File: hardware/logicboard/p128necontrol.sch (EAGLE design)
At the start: 32 parts, among them IC1 74LS595N, IC2 74LS595N, IC3 74LS595N, IC4 74LS595N, IC5 74LS595N, IC6 74LS595N, IC7 74LS595N, IC8 74LS595N

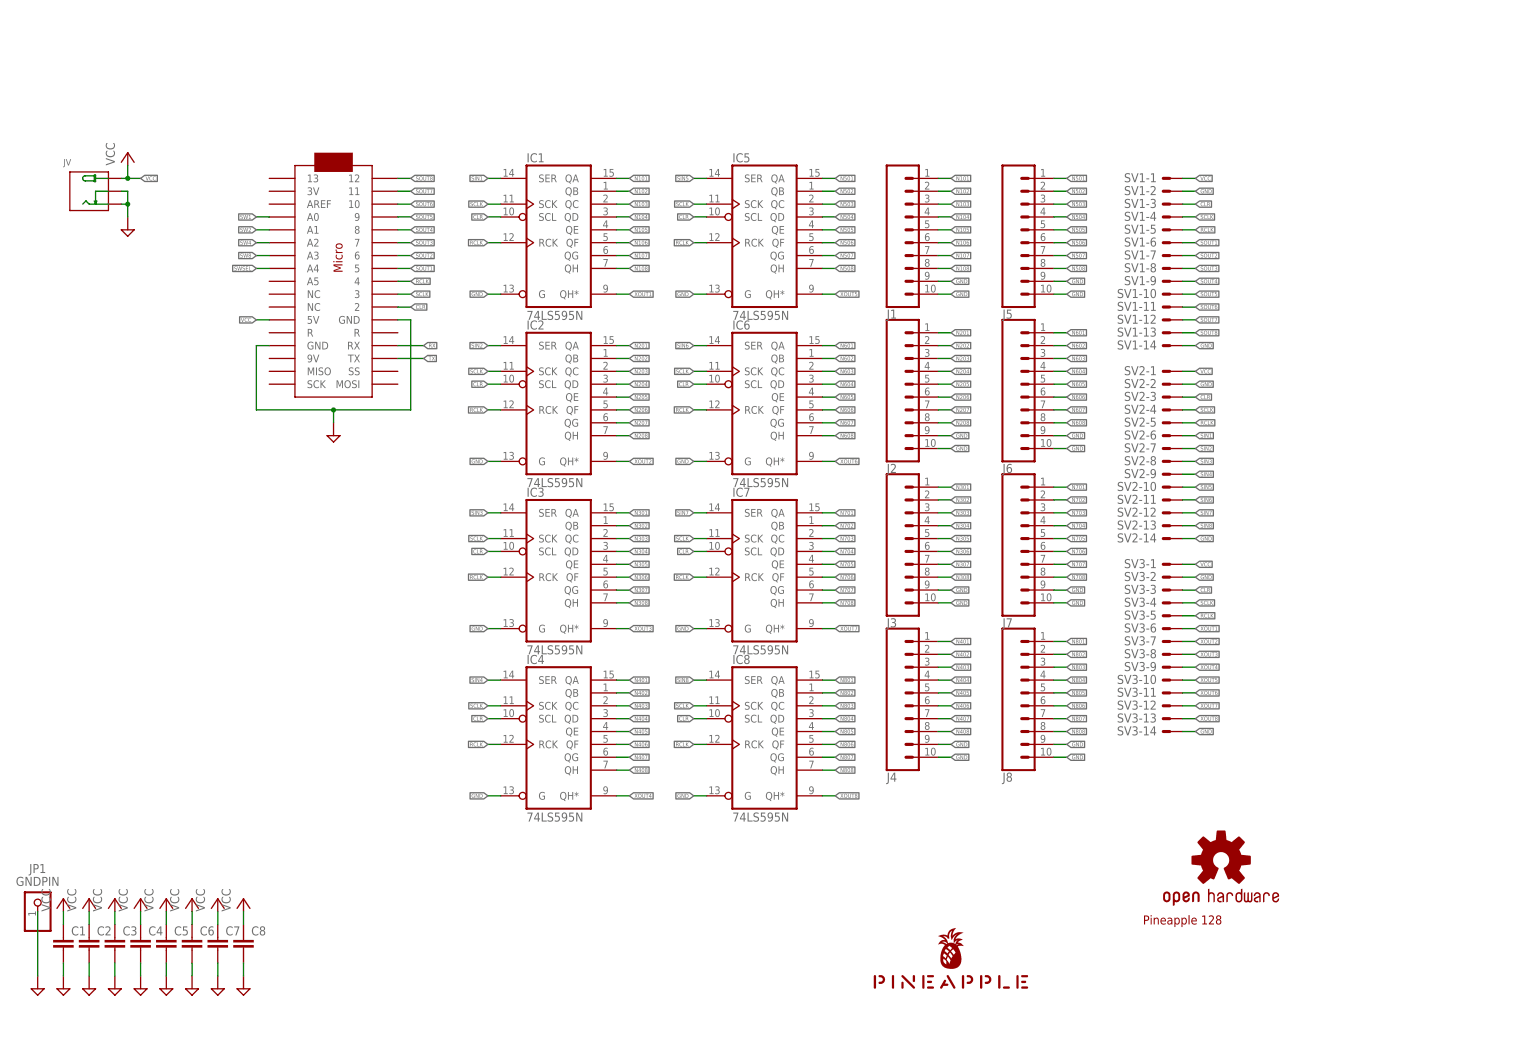
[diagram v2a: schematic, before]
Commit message: Compiled Necontrol.
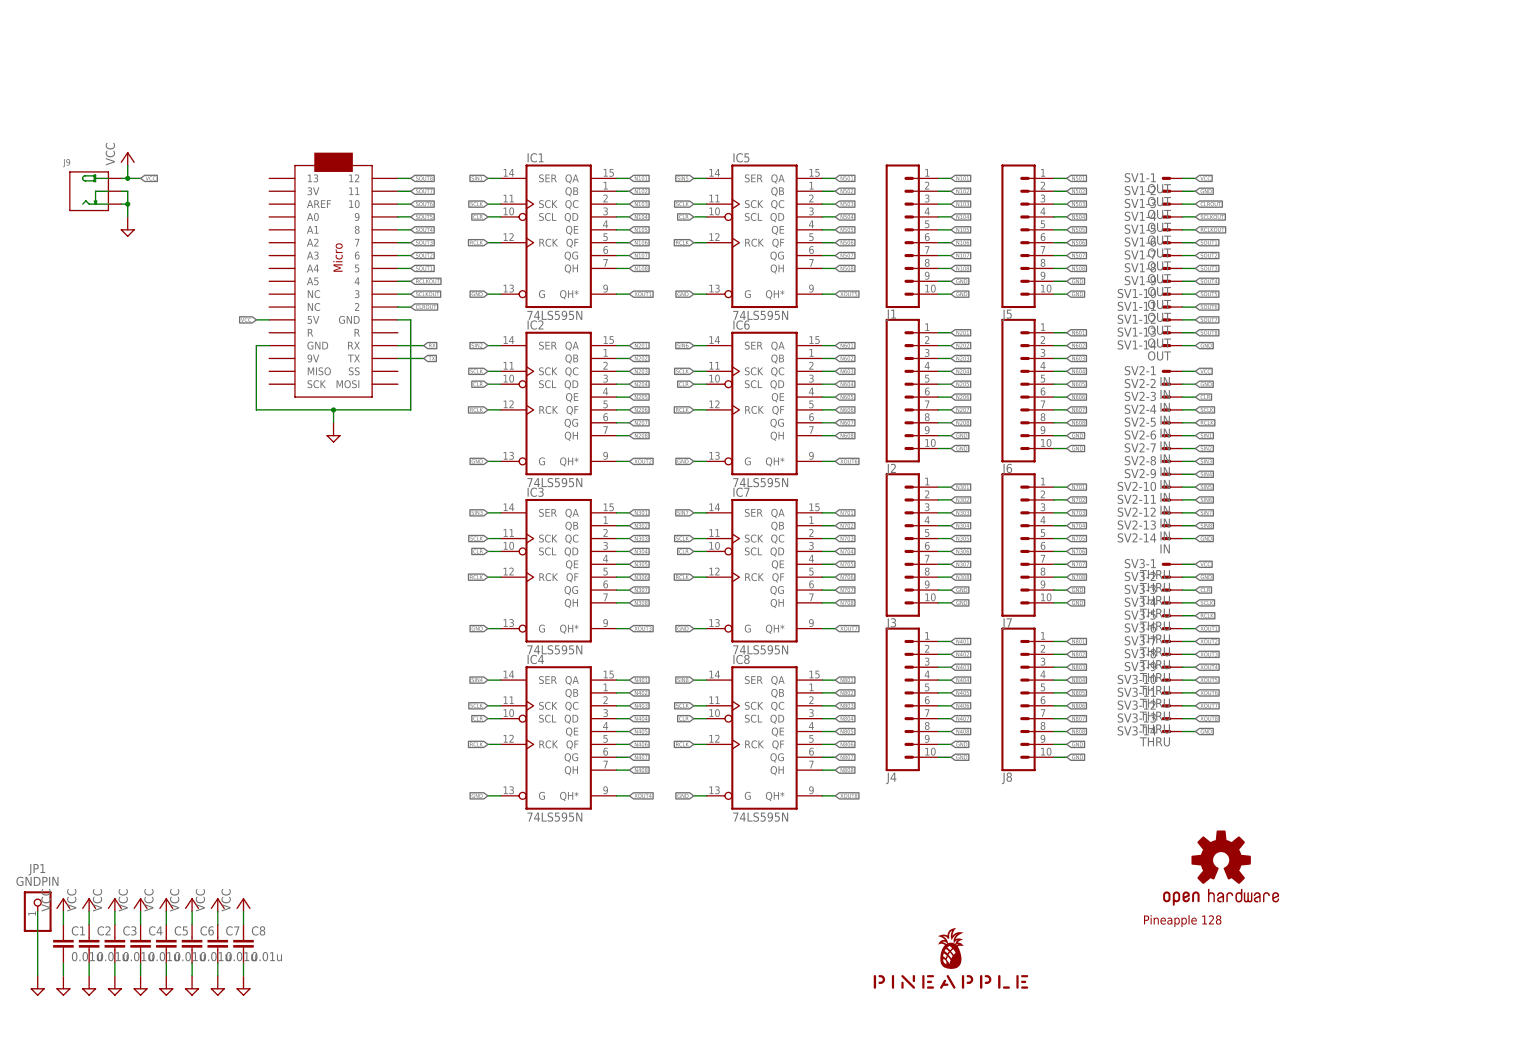
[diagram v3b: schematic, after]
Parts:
- C1, C2, C3, C4, C5, C6, C7, C8: value (none) -> 0.01u
- SV1: value (none) -> OUT
- SV2: value (none) -> IN
- SV3: value (none) -> THRU
- renumbered JV to J9
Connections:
- removed net SW1: U$2.A0
- removed net SW2: U$2.A1
- removed net SW4: U$2.A2
- removed net SW8: U$2.A3
- removed net SWSEL: U$2.A4
- new net CLROUT: SV1-3.S, U$2.2
- new net RCLKOUT: SV1-5.S, U$2.4
- new net SCLKOUT: SV1-4.S, U$2.3
- net CLR: no longer SV1-3.S, U$2.2
- net RCLK: no longer SV1-5.S, U$2.4
- net SCLK: no longer SV1-4.S, U$2.3

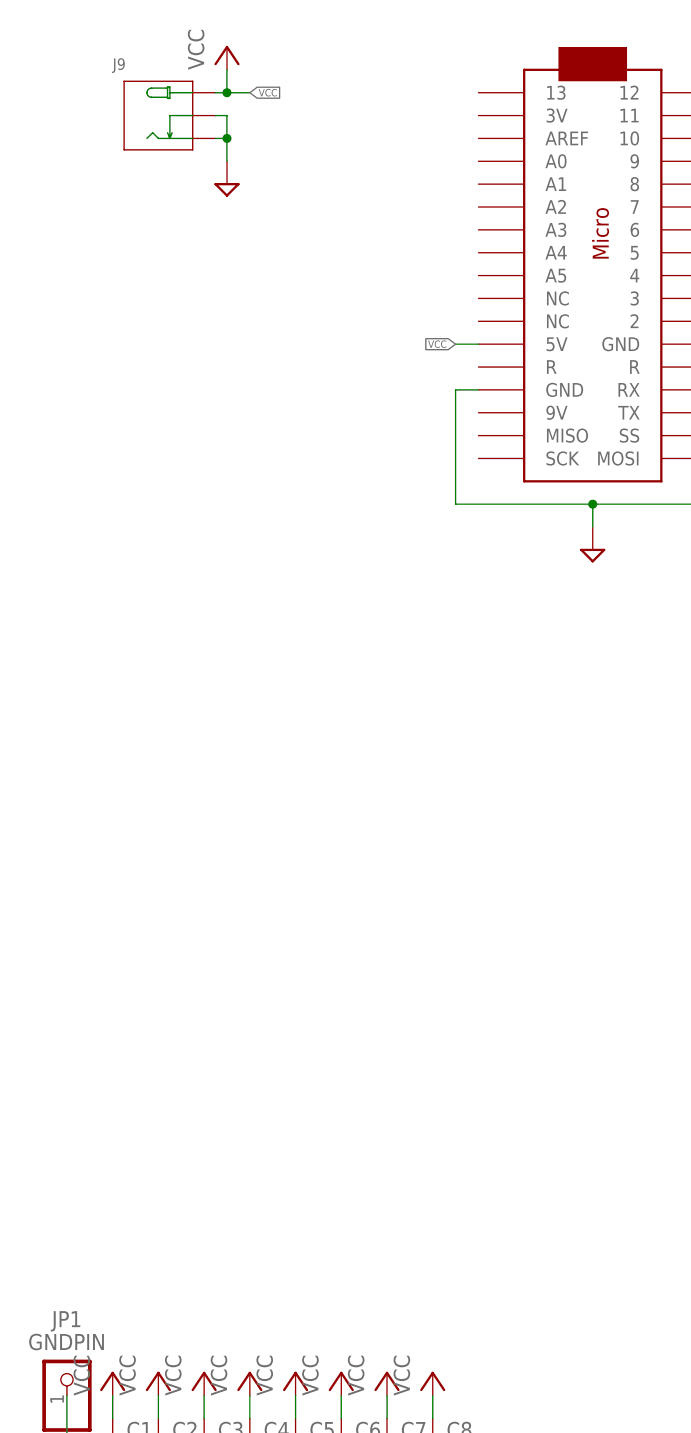
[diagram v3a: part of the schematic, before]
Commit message: Now necontroler (Necobit Controler) has LED indicator.
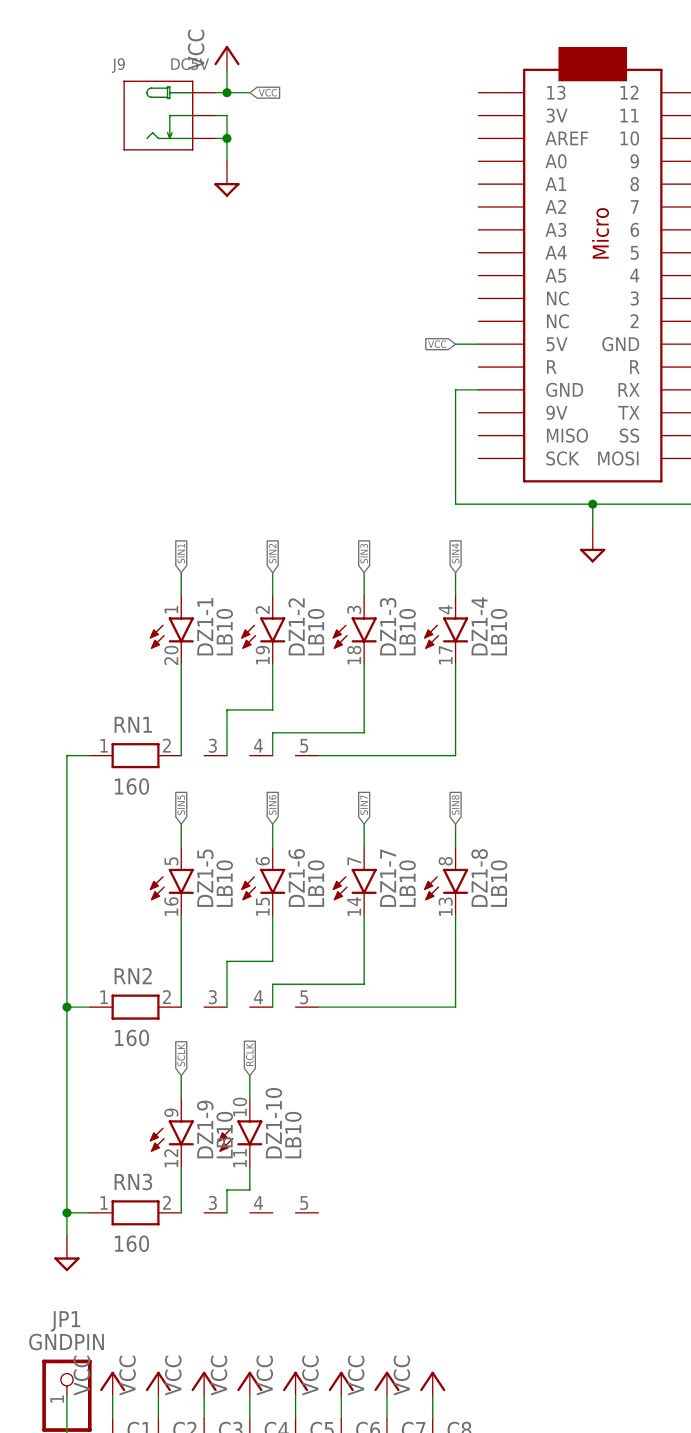
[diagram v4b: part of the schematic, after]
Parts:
- added DZ1: LB10, led:LB10
- added RN1, RN2, RN3: 160, resistor-net:RN04
- J9: value (none) -> DC5V
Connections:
- new net N$1: DZ1-1.C, RN1.2
- new net N$10: DZ1-10.C, RN3.3
- new net N$2: DZ1-2.C, RN1.3
- new net N$3: DZ1-3.C, RN1.4
- new net N$4: DZ1-4.C, RN1.5
- new net N$5: DZ1-5.C, RN2.2
- new net N$6: DZ1-6.C, RN2.3
- new net N$7: DZ1-7.C, RN2.4
- new net N$8: DZ1-8.C, RN2.5
- new net N$9: DZ1-9.C, RN3.2
- net GND: now also RN1.1, RN2.1, RN3.1
- net RCLK: now also DZ1-10.A
- net SCLK: now also DZ1-9.A
- net SIN1: now also DZ1-1.A
- net SIN2: now also DZ1-2.A
- net SIN3: now also DZ1-3.A
- net SIN4: now also DZ1-4.A
- net SIN5: now also DZ1-5.A
- net SIN6: now also DZ1-6.A
- net SIN7: now also DZ1-7.A
- net SIN8: now also DZ1-8.A
